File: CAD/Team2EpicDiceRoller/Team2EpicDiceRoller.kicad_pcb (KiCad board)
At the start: 2 copper layers, 90 x 110 mm, 72 parts, among them J1 Conn_02x03_Odd_Even, J2 Conn_01x16, J3 Barrel_Jack, Q1 BSS138, SW1 SW_Toggle_SPDT, SW2 Tilt_Switch, SW3 SW_Power, SW4 RotaryEncoder_Switch, SW5 SW_LeftMenu, SW6 SW_MidMenu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

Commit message: updated layout, footprints look good
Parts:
- added C18: 100n, Capacitor_SMD:C_1206_3216Metric_Pad1.33x1.80mm_HandSolder, B.Cu at (121.8, 91.7)
- added D3: SB140TA, Diode_THT:D_DO-41_SOD81_P10.16mm_Horizontal, F.Cu at (110.6, 33.3)
- added D4: SB140TA, Diode_THT:D_DO-41_SOD81_P10.16mm_Horizontal, F.Cu at (150.4, 33.3)
- L1, L2: footprint Inductor_SMD:L_0805_2012Metric_Pad1.15x1.40mm_HandSolder -> Inductor_SMD:L_1210_3225Metric_Pad1.42x2.65mm_HandSolder
- R12, R13: footprint Resistor_SMD:R_1206_3216Metric_Pad1.30x1.75mm_HandSolder -> Resistor_SMD:R_2512_6332Metric_Pad1.40x3.35mm_HandSolder
- moved R13 3.81 mm to (175.6, 90.8)
- moved R12 2.18 mm to (104.8, 101.8)
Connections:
- Q1 pad 2: IO8_PB0 -> LCD_RX
- Q1 pad 3: LCD_RX -> IO8_PB0
- R14 pad 2: IO8_PB0 -> LCD_RX
- R16 pad 2: LCD_RX -> IO8_PB0

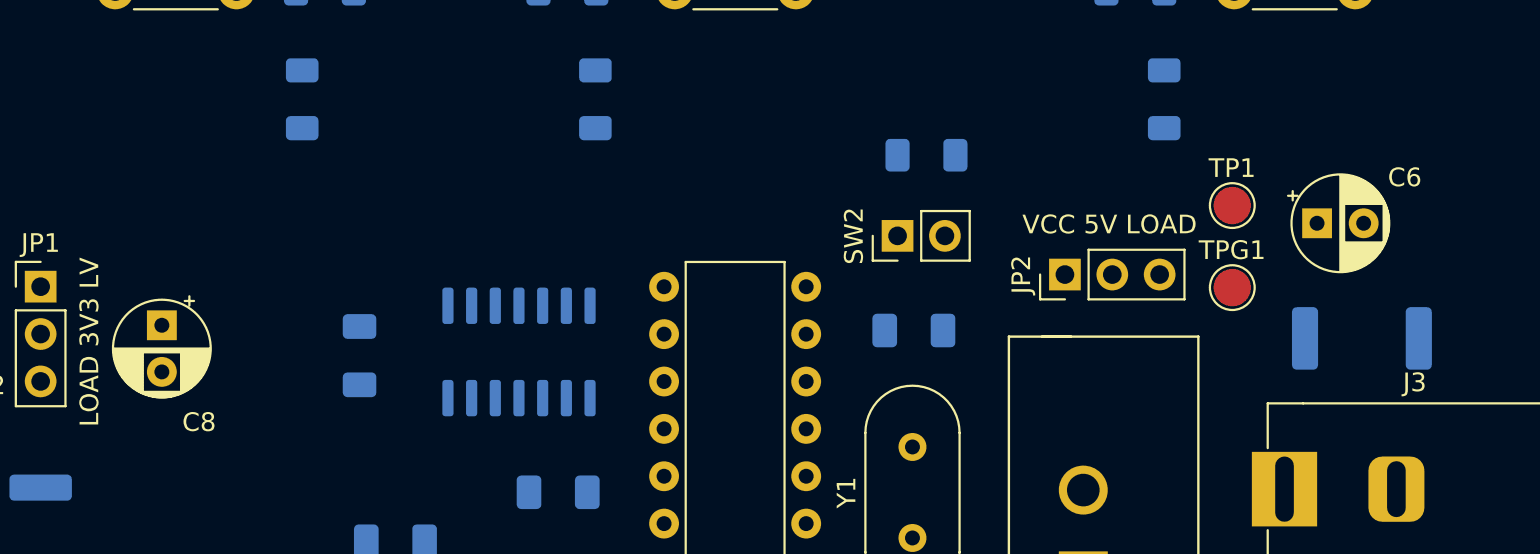
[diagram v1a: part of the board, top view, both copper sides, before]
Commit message: Replaced footprint for 470uF cap
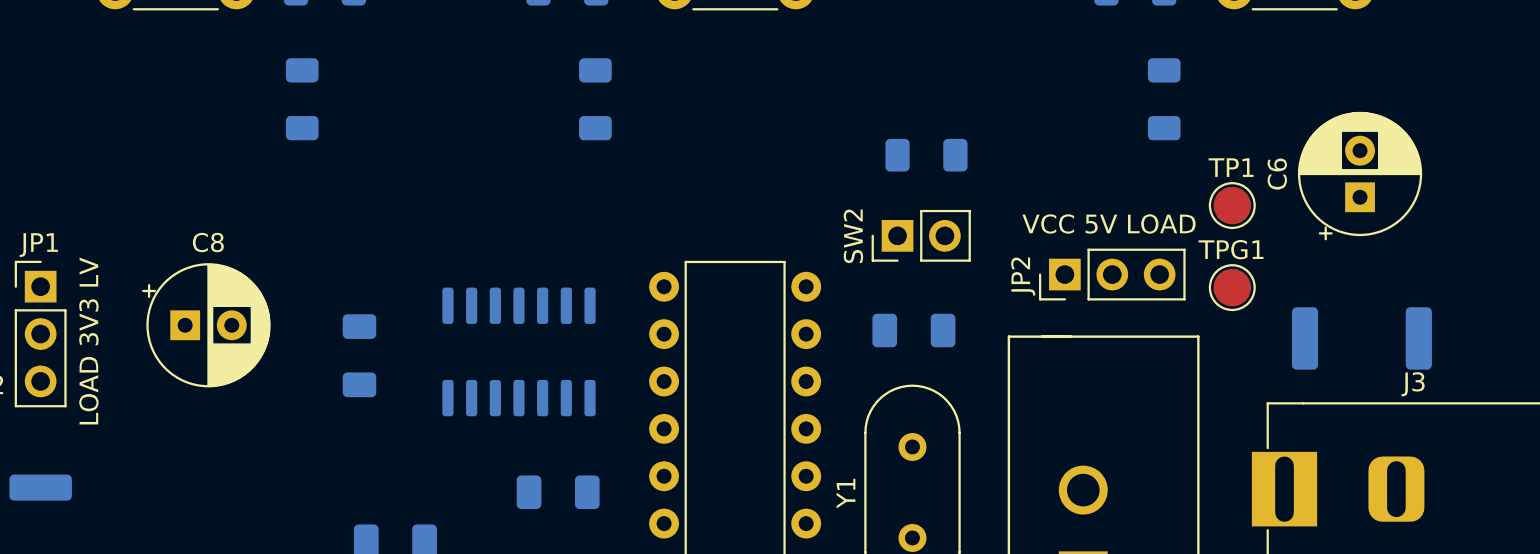
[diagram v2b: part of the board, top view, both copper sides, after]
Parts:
- C6, C8: footprint Capacitor_THT:CP_Radial_D5.0mm_P2.50mm -> Capacitor_THT:CP_Radial_D6.3mm_P2.50mm
- moved C6 2.69 mm to (175.5, 83.2), turned to 90 degrees
- moved C8 1.25 mm to (112.5, 90.0), turned to 0 degrees

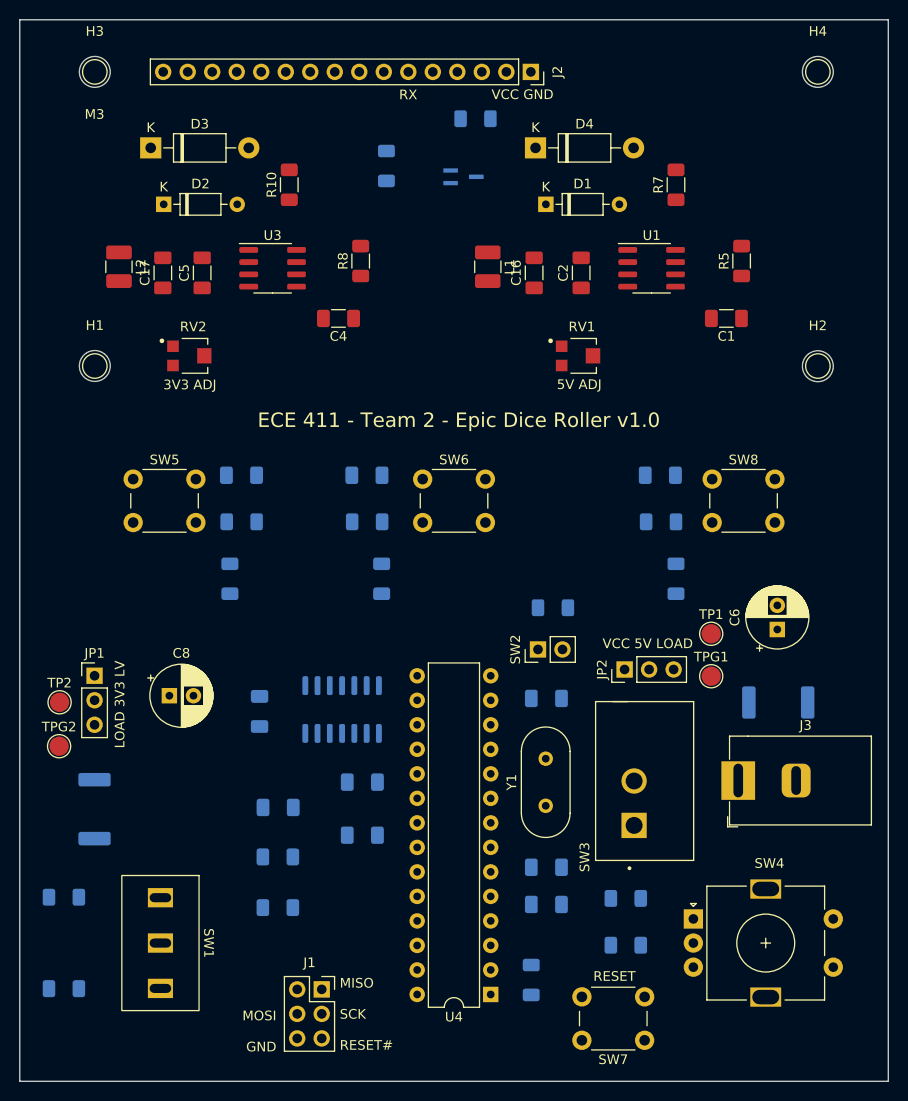
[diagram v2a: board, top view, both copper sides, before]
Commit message: Added mounting holes, updated general layout of pcb for routing
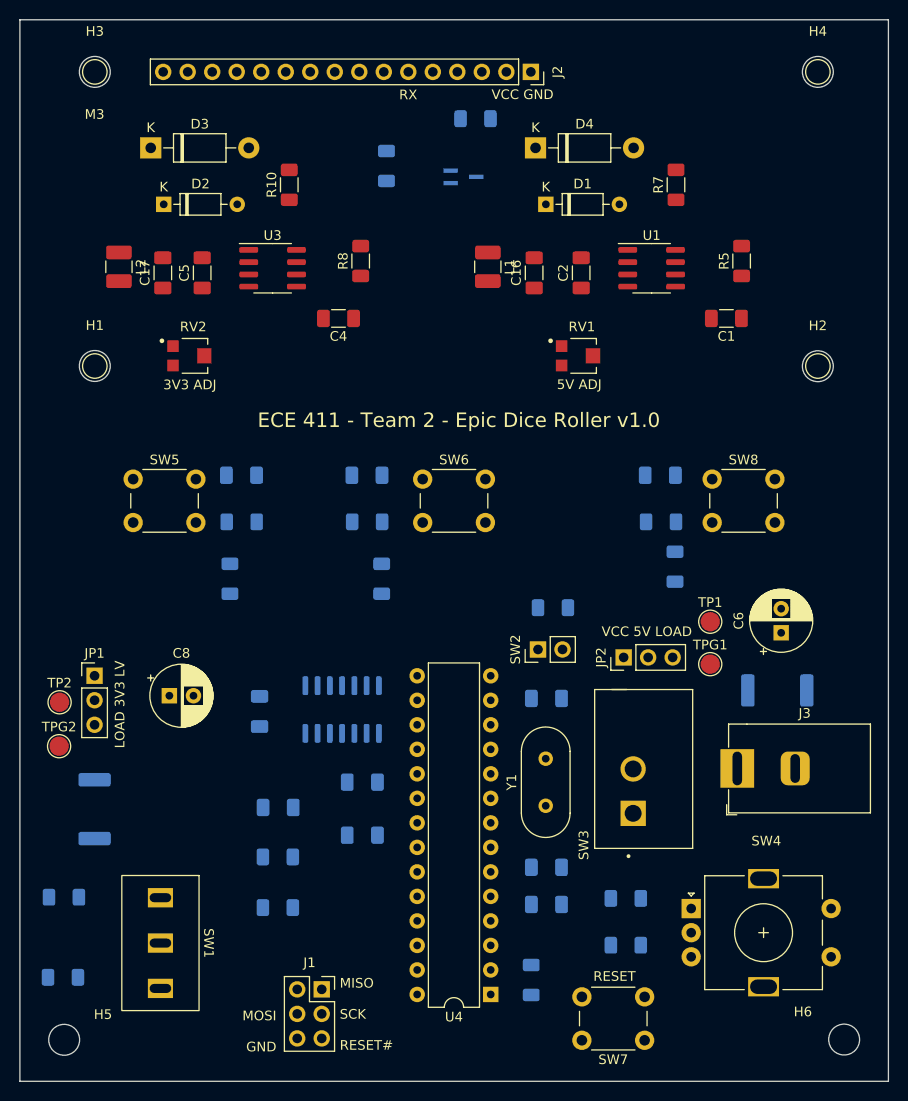
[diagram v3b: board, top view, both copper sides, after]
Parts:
- added H5: MountingHole, MountingHole:MountingHole_3.2mm_M3, F.Cu at (101.6, 125.7)
- added H6: MountingHole, MountingHole:MountingHole_3.2mm_M3, F.Cu at (182.4, 125.7)
- moved JP2 1.25 mm to (159.6, 86.1)
- moved J3 1.25 mm to (171.3, 97.6)
- moved R13 1.25 mm to (175.5, 89.5)
- moved R19 1.25 mm to (164.9, 76.7)
- moved SW3 1.25 mm to (161.7, 97.6)
- moved TP1 1.25 mm to (168.6, 82.4)
- moved TPG1 1.25 mm to (168.6, 86.8)
- moved R2 1.18 mm to (101.5, 119.2)
- moved SW4 1.10 mm to (166.6, 112.1)
- moved C6 0.53 mm to (175.9, 83.5)
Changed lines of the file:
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@@
   )
   (footprint "Library:BarrelJack_CUI_PJ-037A_Horizontal" (layer "F.Cu")
-    (at 171.45 98.8325 180)
+    (at 171.35 97.5825 180)
     (descr "DC Barrel Jack")
     (tags "Power Jack")
@@
   )
   (footprint "TestPoint:TestPoint_Pad_D2.0mm" (layer "F.Cu")
-    (at 168.65 83.625)
+    (at 168.55 82.375)
     (descr "SMD pad as test Point, diameter 2.0mm")
     (tags "test point SMD pad")
@@
   )
   (footprint "TestPoint:TestPoint_Pad_D2.0mm" (layer "F.Cu")
-    (at 168.65 88.025)
+    (at 168.55 86.775)
     (descr "SMD pad as test Point, diameter 2.0mm")
     (tags "test point SMD pad")
@@
     )
   )
+  (footprint "MountingHole:MountingHole_3.2mm_M3" (layer "F.Cu")
+    (at 101.6 125.7)
+    (descr "Mounting Hole 3.2mm, no annular, M3")
+    (tags "mounting hole 3.2mm no annular m3")
+    (property "Sheetfile" "Team2EpicDiceRoller.kicad_sch")
+    (property "Sheetname" "")
+    (attr exclude_from_pos_files)
+    (fp_text reference "H5" (at 4.025 -2.625) (layer "F.SilkS")
+      (effects (font (size 1 1) (thickness 0.15)))
+    )
+    (fp_text value "MountingHole" (at 0 4.2) (layer "F.Fab")
+      (effects (font (size 1 1) (thickness 0.15)))
+    )
+    (fp_text user "${REFERENCE}" (at 0.3 0) (layer "F.Fab")
+      (effects (font (size 1 1) (thickness 0.15)))
+    )
+    (fp_circle (center 0 0) (end 3.2 0) (layer "Cmts.User") (width 0.15) (fill none))
+    (fp_circle (center 0 0) (end 3.45 0) (layer "F.CrtYd") (width 0.05) (fill none))
+    (pad "" np_thru_hole circle locked (at 0 0) (size 3.2 3.2) (drill 3.2) (layers *.Cu *.Mask))
+  )
   (footprint "Inductor_SMD:L_1210_3225Metric_Pad1.42x2.65mm_HandSolder" (layer "F.Cu")
     (at 145.5 45.595 -90)
@@
   )
   (footprint "Capacitor_THT:CP_Radial_D6.3mm_P2.50mm" (layer "F.Cu")
-    (at 175.5 83.18238 90)
+    (at 175.9 83.525 90)
     (descr "CP, Radial series, Radial, pin pitch=2.50mm, , diameter=6.3mm, Electrolytic Capacitor")
     (tags "CP Radial series Radial pin pitch 2.50mm  diameter 6.3mm Electrolytic Capacitor")
@@
     (fp_circle (center 1.25 0) (end 4.4 0) (layer "F.Fab") (width 0.1) (fill none))
     (pad "1" thru_hole rect locked (at 0 0 90) (size 1.6 1.6) (drill 0.8) (layers *.Cu *.Mask)
-      (net 4 "VCC"))
+      (net 4 "VCC") (pintype "passive"))
     (pad "2" thru_hole circle locked (at 2.5 0 90) (size 1.6 1.6) (drill 0.8) (layers *.Cu *.Mask)
-      (net 1 "GND"))
+      (net 1 "GND") (pintype "passive"))
     (model "${KICAD6_3DMODEL_DIR}/Capacitor_THT.3dshapes/CP_Radial_D6.3mm_P2.50mm.wrl"
       (offset (xyz 0 0 0))
@@
   )
   (footprint "GF-123-0054:SW_GF-123-0054" (layer "F.Cu")
-    (at 161.75 98.8825 90)
+    (at 161.65 97.6325 90)
     (property "Sheetfile" "Team2EpicDiceRoller.kicad_sch")
     (property "Sheetname" "")
@@
   )
   (footprint "Rotary_Encoder:RotaryEncoder_Alps_EC11E-Switch_Vertical_H20mm" (layer "F.Cu")
-    (at 166.8 113.175)
+    (at 166.575 112.1)
     (descr "Alps rotary encoder, EC12E... with switch, vertical shaft, http://www.alps.com/prod/info/E/HTML/Encoder/Incremental/EC11/EC11E15204A3.html")
     (tags "rotary encoder")
@@
     (property "Sheetname" "")
     (attr through_hole)
-    (fp_text reference "SW4" (at 7.885 -5.755) (layer "F.SilkS")
+    (fp_text reference "SW4" (at 7.785 -7.005) (layer "F.SilkS")
       (effects (font (size 1 1) (thickness 0.15)))
     )
@@
   )
   (footprint "Connector_PinHeader_2.54mm:PinHeader_1x03_P2.54mm_Vertical" (layer "F.Cu")
-    (at 159.675 87.325 90)
+    (at 159.575 86.075 90)
     (descr "Through hole straight pin header, 1x03, 2.54mm pitch, single row")
     (tags "Through hole pin header THT 1x03 2.54mm single row")
@@
     )
   )
+  (footprint "MountingHole:MountingHole_3.2mm_M3" (layer "F.Cu")
+    (at 182.425 125.675)
+    (descr "Mounting Hole 3.2mm, no annular, M3")
+    (tags "mounting hole 3.2mm no annular m3")
+    (property "Sheetfile" "Team2EpicDiceRoller.kicad_sch")
+    (property "Sheetname" "")
+    (attr exclude_from_pos_files)
+    (fp_text reference "H6" (at -4.275 -2.875) (layer "F.SilkS")
+      (effects (font (size 1 1) (thickness 0.15)))
+    )
+    (fp_text value "MountingHole" (at 0 4.2) (layer "F.Fab")
+      (effects (font (size 1 1) (thickness 0.15)))
+    )
+    (fp_text user "${REFERENCE}" (at 0.3 0) (layer "F.Fab")
+      (effects (font (size 1 1) (thickness 0.15)))
+    )
+    (fp_circle (center 0 0) (end 3.2 0) (layer "Cmts.User") (width 0.15) (fill none))
+    (fp_circle (center 0 0) (end 3.45 0) (layer "F.CrtYd") (width 0.05) (fill none))
+    (pad "" np_thru_hole circle locked (at 0 0) (size 3.2 3.2) (drill 3.2) (layers *.Cu *.Mask))
+  )
   (footprint "Capacitor_SMD:C_1206_3216Metric_Pad1.33x1.80mm_HandSolder" (layer "F.Cu")
     (at 115.9 46.225 90)
@@
   )
   (footprint "Resistor_SMD:R_1206_3216Metric_Pad1.30x1.75mm_HandSolder" (layer "B.Cu")
-    (at 165 77.925 90)
+    (at 164.9 76.675 90)
     (descr "Resistor SMD 1206 (3216 Metric), square (rectangular) end terminal, IPC_7351 nominal with elongated pad for handsoldering. (Body size source: IPC-SM-782 page 72, https://www.pcb-3d.com/wordpress/wp-content/uploads/ipc-sm-782a_amendment_1_and_2.pdf), generated with kicad-footprint-generator")
     (tags "resistor handsolder")
@@
   )
   (footprint "Resistor_SMD:R_1206_3216Metric_Pad1.30x1.75mm_HandSolder" (layer "B.Cu")
-    (at 101.575 120.4)
+    (at 101.475 119.225)
     (descr "Resistor SMD 1206 (3216 Metric), square (rectangular) end terminal, IPC_7351 nominal with elongated pad for handsoldering. (Body size source: IPC-SM-782 page 72, https://www.pcb-3d.com/wordpress/wp-content/uploads/ipc-sm-782a_amendment_1_and_2.pdf), generated with kicad-footprint-generator")
     (tags "resistor handsolder")
@@
     (property "Sheetname" "")
     (attr smd)
-    (fp_text reference "R2" (at 0 1.82) (layer "B.SilkS")
+    (fp_text reference "R2" (at 0 -1.925) (layer "B.SilkS")
       (effects (font (size 1 1) (thickness 0.15)) (justify mirror))
     )
-    (fp_text value "10k" (at 0 -1.82) (layer "B.Fab")
+    (fp_text value "10k" (at 0.025 1.8) (layer "B.Fab")
       (effects (font (size 1 1) (thickness 0.15)) (justify mirror))
     )
-    (fp_text user "${REFERENCE}" (at 0 0) (layer "B.Fab")
+    (fp_text user "${REFERENCE}" (at -0.025 -0.025) (layer "B.Fab")
       (effects (font (size 0.8 0.8) (thickness 0.12)) (justify mirror))
     )
@@
   )
   (footprint "Resistor_SMD:R_2512_6332Metric_Pad1.40x3.35mm_HandSolder" (layer "B.Cu")
-    (at 175.6 90.75)
+    (at 175.5 89.5)
     (descr "Resistor SMD 2512 (6332 Metric), square (rectangular) end terminal, IPC_7351 nominal with elongated pad for handsoldering. (Body size source: IPC-SM-782 page 72, https://www.pcb-3d.com/wordpress/wp-content/uploads/ipc-sm-782a_amendment_1_and_2.pdf), generated with kicad-footprint-generator")
     (tags "resistor handsolder")
@@
     (property "Sheetname" "")
     (attr smd)
-    (fp_text reference "R3" (at -0.025 2.125) (layer "B.SilkS")
+    (fp_text reference "R3" (at -0.05 -1.875) (layer "B.SilkS")
       (effects (font (size 1 1) (thickness 0.15)) (justify mirror))
     )
-    (fp_text value "10k" (at 0 -1.82) (layer "B.Fab")
+    (fp_text value "10k" (at -0.025 1.725) (layer "B.Fab")
       (effects (font (size 1 1) (thickness 0.15)) (justify mirror))
     )
@@
     )
   )
-  (gr_rect (start 97 20) (end 187 130) (layer "Edge.Cuts") (width 0.1) (fill none))
+  (gr_rect (start 97.0125 20) (end 187.0125 130) (layer "Edge.Cuts") (width 0.1) (fill none))
   (gr_text "3V3 ADJ" (at 114.625 57.825) (layer "F.SilkS")
     (effects (font (size 1 1) (thickness 0.15)))
@@
     (effects (font (size 1.5 1.5) (thickness 0.3)))
   )
-  (gr_text "VCC 5V LOAD" (at 162.075 84.65) (layer "F.SilkS")
+  (gr_text "VCC 5V LOAD" (at 161.975 83.4) (layer "F.SilkS")
     (effects (font (size 1 1) (thickness 0.15)))
   )

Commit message: Updated pin selections for some of the io so that we can use the screen and the enableinterrupt library at the same time
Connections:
- Q1 pad 3: IO8_PB0 -> IO9_PB1
- R1 pad 2: IO9_PB1 -> IO7_PD7
- R16 pad 2: IO8_PB0 -> IO9_PB1
- R2 pad 2: AD1_PC1 -> AD3_PC3
- R3 pad 2: AD0_PC0 -> AD2_PC2
- SW1 pad 1: AD0_PC0 -> AD2_PC2
- SW1 pad 3: AD1_PC1 -> AD3_PC3
- SW2 pad 1: IO9_PB1 -> IO7_PD7
- U2 pad 6: IO7_PD7 -> IO10_SS_PB2
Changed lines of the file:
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@@
     (fp_line (start -0.635 -1.27) (end 1.27 -1.27) (layer "F.Fab") (width 0.1))
     (pad "1" thru_hole rect locked (at 0 0 90) (size 1.7 1.7) (drill 1) (layers *.Cu *.Mask)
-      (net 27 "IO9_PB1") (pinfunction "1") (pintype "passive"))
+      (net 38 "IO7_PD7") (pinfunction "1") (pintype "passive"))
     (pad "2" thru_hole oval locked (at 0 2.54 90) (size 1.7 1.7) (drill 1) (layers *.Cu *.Mask)
       (net 1 "GND") (pinfunction "2") (pintype "passive"))
@@
     (fp_line (start 6.4 -3.4) (end 6.4 3.4) (layer "F.Fab") (width 0.12))
     (pad "1" thru_hole rect (at -4.7 0 270) (size 2 2.6) (drill oval 0.95 2.25) (layers *.Cu *.Mask)
-      (net 29 "AD0_PC0") (pinfunction "A") (pintype "passive"))
+      (net 42 "AD2_PC2") (pinfunction "A") (pintype "passive"))
     (pad "2" thru_hole rect (at 0 0 270) (size 2 2.6) (drill oval 0.95 2.25) (layers *.Cu *.Mask)
       (net 1 "GND") (pinfunction "B") (pintype "passive"))
     (pad "3" thru_hole rect (at 4.7 0 270) (size 2 2.6) (drill oval 0.95 2.25) (layers *.Cu *.Mask)
-      (net 28 "AD1_PC1") (pinfunction "C") (pintype "passive"))
+      (net 43 "AD3_PC3") (pinfunction "C") (pintype "passive"))
   )
   (footprint "Resistor_SMD:R_1206_3216Metric_Pad1.30x1.75mm_HandSolder" (layer "B.Cu")
@@
       (net 4 "VCC") (pintype "passive"))
     (pad "2" smd roundrect locked (at 1.55 0 180) (size 1.3 1.75) (layers "B.Cu" "B.Paste" "B.Mask") (roundrect_rratio 0.192308)
-      (net 27 "IO9_PB1") (pintype "passive"))
+      (net 38 "IO7_PD7") (pintype "passive"))
     (model "${KICAD6_3DMODEL_DIR}/Resistor_SMD.3dshapes/R_1206_3216Metric.wrl"
       (offset (xyz 0 0 0))
@@
       (net 51 "LCD_RX") (pinfunction "S") (pintype "passive"))
     (pad "3" smd rect locked (at 1.33 0 90) (size 0.45 1.5) (layers "B.Cu" "B.Paste" "B.Mask")
-      (net 16 "IO8_PB0") (pinfunction "D") (pintype "passive"))
+      (net 27 "IO9_PB1") (pinfunction "D") (pintype "passive"))
     (model "${KICAD6_3DMODEL_DIR}/Package_TO_SOT_SMD.3dshapes/SOT-323_SC-70.wrl"
       (offset (xyz 0 0 0))
@@
       (net 4 "VCC") (pintype "passive"))
     (pad "2" smd roundrect locked (at 1.55 0 180) (size 1.3 1.75) (layers "B.Cu" "B.Paste" "B.Mask") (roundrect_rratio 0.192308)
-      (net 16 "IO8_PB0") (pintype "passive"))
+      (net 27 "IO9_PB1") (pintype "passive"))
     (model "${KICAD6_3DMODEL_DIR}/Resistor_SMD.3dshapes/R_1206_3216Metric.wrl"
       (offset (xyz 0 0 0))
@@
       (net 4 "VCC") (pintype "passive"))
     (pad "2" smd roundrect locked (at 1.55 0) (size 1.3 1.75) (layers "B.Cu" "B.Paste" "B.Mask") (roundrect_rratio 0.192308)
-      (net 28 "AD1_PC1") (pintype "passive"))
+      (net 43 "AD3_PC3") (pintype "passive"))
     (model "${KICAD6_3DMODEL_DIR}/Resistor_SMD.3dshapes/R_1206_3216Metric.wrl"
       (offset (xyz 0 0 0))
@@
       (net 4 "VCC") (pintype "passive"))
     (pad "2" smd roundrect locked (at 1.55 0) (size 1.3 1.75) (layers "B.Cu" "B.Paste" "B.Mask") (roundrect_rratio 0.192308)
-      (net 29 "AD0_PC0") (pintype "passive"))
+      (net 42 "AD2_PC2") (pintype "passive"))
     (model "${KICAD6_3DMODEL_DIR}/Resistor_SMD.3dshapes/R_1206_3216Metric.wrl"
       (offset (xyz 0 0 0))
@@
       (net 64 "/RigDebn") (pintype "input"))
     (pad "6" smd roundrect locked (at -2.475 -2.54 270) (size 1.95 0.6) (layers "B.Cu" "B.Paste" "B.Mask") (roundrect_rratio 0.25)
-      (net 38 "IO7_PD7") (pintype "output"))
+      (net 40 "IO10_SS_PB2") (pintype "output"))
     (pad "7" smd roundrect locked (at -2.475 -3.81 270) (size 1.95 0.6) (layers "B.Cu" "B.Paste" "B.Mask") (roundrect_rratio 0.25)
       (net 1 "GND") (pinfunction "GND") (pintype "power_in"))
